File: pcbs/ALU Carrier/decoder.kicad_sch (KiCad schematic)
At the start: 19 parts, among them U2001 74HC138, U2002 74HC14, U2003 74HC08

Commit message: Fix indicators
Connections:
- net +5V: now also D2001.2 (A), D2002.2 (A), D2003.2 (A), D2004.2 (A), D2005.2 (A), D2006.2 (A), D2007.2 (A), D2008.2 (A)
- net GND: no longer D2001.1 (K), D2002.1 (K), D2003.1 (K), D2004.1 (K), D2005.1 (K), D2006.1 (K), D2007.1 (K), D2008.1 (K)
- net at R2005.1: now also D2005.1 (K); no longer D2005.2 (A)
- net at R2006.1: now also D2006.1 (K); no longer D2006.2 (A)
- net at R2004.1: now also D2004.1 (K); no longer D2004.2 (A)
- net at R2007.1: now also D2007.1 (K); no longer D2007.2 (A)
- net at R2008.1: now also D2008.1 (K); no longer D2008.2 (A)
- net at R2001.1: now also D2001.1 (K); no longer D2001.2 (A)
- net at R2002.1: now also D2002.1 (K); no longer D2002.2 (A)
- net at R2003.1: now also D2003.1 (K); no longer D2003.2 (A)
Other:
- moved on the sheet: D2001, D2002, D2003, D2004, D2005, D2006, D2007, D2008
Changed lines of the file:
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@@
 	(symbol
 		(lib_id "Device:LED")
-		(at 152.4 90.17 90)
+		(at 152.4 90.17 270)
 		(unit 1)
 		(exclude_from_sim no)
@@
 		(fields_autoplaced yes)
 		(property "Reference" "D2005"
-			(at 159.385 91.7575 0)
-			(effects
-				(font
-					(size 1.27 1.27)
-				)
+			(at 154.94 87.3124 90)
+			(effects
+				(font
+					(size 1.27 1.27)
+				)
+				(justify left)
 			)
 		)
 		(property "Value" "Blue"
-			(at 156.845 91.7575 0)
-			(effects
-				(font
-					(size 1.27 1.27)
-				)
+			(at 154.94 89.8524 90)
+			(effects
+				(font
+					(size 1.27 1.27)
+				)
+				(justify left)
 			)
 		)
@@
 	(symbol
 		(lib_id "Device:LED")
-		(at 165.1 90.17 90)
+		(at 165.1 90.17 270)
 		(unit 1)
 		(exclude_from_sim no)
@@
 		(fields_autoplaced yes)
 		(property "Reference" "D2006"
-			(at 172.085 91.7575 0)
-			(effects
-				(font
-					(size 1.27 1.27)
-				)
+			(at 167.64 87.3124 90)
+			(effects
+				(font
+					(size 1.27 1.27)
+				)
+				(justify left)
 			)
 		)
 		(property "Value" "Blue"
-			(at 169.545 91.7575 0)
-			(effects
-				(font
-					(size 1.27 1.27)
-				)
+			(at 167.64 89.8524 90)
+			(effects
+				(font
+					(size 1.27 1.27)
+				)
+				(justify left)
 			)
 		)
@@
 				(path "/2be9e5f9-941e-4c29-a733-4c8d2e8b8610/76c82fde-9a27-48e2-82d2-e603579339ec"
 					(reference "D2006")
-					(unit 1)
-				)
-			)
-		)
-	)
-	(symbol
-		(lib_id "power:GND")
-		(at 101.6 101.6 0)
-		(unit 1)
-		(exclude_from_sim no)
-		(in_bom yes)
-		(on_board yes)
-		(dnp no)
-		(fields_autoplaced yes)
-		(property "Reference" "#PWR02003"
-			(at 101.6 107.95 0)
-			(effects
-				(font
-					(size 1.27 1.27)
-				)
-				(hide yes)
-			)
-		)
-		(property "Value" "GND"
-			(at 101.6 106.68 0)
-			(effects
-				(font
-					(size 1.27 1.27)
-				)
-			)
-		)
-		(property "Footprint" ""
-			(at 101.6 101.6 0)
-			(effects
-				(font
-					(size 1.27 1.27)
-				)
-				(hide yes)
-			)
-		)
-		(property "Datasheet" ""
-			(at 101.6 101.6 0)
-			(effects
-				(font
-					(size 1.27 1.27)
-				)
-				(hide yes)
-			)
-		)
-		(property "Description" "Power symbol creates a global label with name \"GND\" , ground"
-			(at 101.6 101.6 0)
-			(effects
-				(font
-					(size 1.27 1.27)
-				)
-				(hide yes)
-			)
-		)
-		(pin "1"
-		)
-		(instances
-			(project ""
-				(path "/2be9e5f9-941e-4c29-a733-4c8d2e8b8610/76c82fde-9a27-48e2-82d2-e603579339ec"
-					(reference "#PWR02003")
 					(unit 1)
 				)
@@
 	(symbol
 		(lib_id "Device:LED")
-		(at 190.5 90.17 90)
+		(at 190.5 90.17 270)
 		(unit 1)
 		(exclude_from_sim no)
@@
 		(fields_autoplaced yes)
 		(property "Reference" "D2008"
-			(at 197.485 91.7575 0)
-			(effects
-				(font
-					(size 1.27 1.27)
-				)
+			(at 193.04 87.3124 90)
+			(effects
+				(font
+					(size 1.27 1.27)
+				)
+				(justify left)
 			)
 		)
 		(property "Value" "Blue"
-			(at 194.945 91.7575 0)
-			(effects
-				(font
-					(size 1.27 1.27)
-				)
+			(at 193.04 89.8524 90)
+			(effects
+				(font
+					(size 1.27 1.27)
+				)
+				(justify left)
 			)
 		)
@@
 	(symbol
 		(lib_id "Device:LED")
-		(at 101.6 90.17 90)
+		(at 101.6 90.17 270)
 		(unit 1)
 		(exclude_from_sim no)
@@
 		(fields_autoplaced yes)
 		(property "Reference" "D2001"
-			(at 108.585 91.7575 0)
-			(effects
-				(font
-					(size 1.27 1.27)
-				)
+			(at 104.14 87.3124 90)
+			(effects
+				(font
+					(size 1.27 1.27)
+				)
+				(justify left)
 			)
 		)
 		(property "Value" "Blue"
-			(at 106.045 91.7575 0)
-			(effects
-				(font
-					(size 1.27 1.27)
-				)
+			(at 104.14 89.8524 90)
+			(effects
+				(font
+					(size 1.27 1.27)
+				)
+				(justify left)
 			)
 		)
@@
 	)
 	(symbol
+		(lib_id "power:+5V")
+		(at 101.6 101.6 180)
+		(unit 1)
+		(exclude_from_sim no)
+		(in_bom yes)
+		(on_board yes)
+		(dnp no)
+		(fields_autoplaced yes)
+		(property "Reference" "#PWR02003"
+			(at 101.6 97.79 0)
+			(effects
+				(font
+					(size 1.27 1.27)
+				)
+				(hide yes)
+			)
+		)
+		(property "Value" "+5V"
+			(at 101.6 106.68 0)
+			(effects
+				(font
+					(size 1.27 1.27)
+				)
+			)
+		)
+		(property "Footprint" ""
+			(at 101.6 101.6 0)
+			(effects
+				(font
+					(size 1.27 1.27)
+				)
+				(hide yes)
+			)
+		)
+		(property "Datasheet" ""
+			(at 101.6 101.6 0)
+			(effects
+				(font
+					(size 1.27 1.27)
+				)
+				(hide yes)
+			)
+		)
+		(property "Description" "Power symbol creates a global label with name \"+5V\""
+			(at 101.6 101.6 0)
+			(effects
+				(font
+					(size 1.27 1.27)
+				)
+				(hide yes)
+			)
+		)
+		(pin "1"
+		)
+		(instances
+			(project "ALU Carrier"
+				(path "/2be9e5f9-941e-4c29-a733-4c8d2e8b8610/76c82fde-9a27-48e2-82d2-e603579339ec"
+					(reference "#PWR02003")
+					(unit 1)
+				)
+			)
+		)
+	)
+	(symbol
 		(lib_id "Device:LED")
-		(at 139.7 90.17 90)
+		(at 139.7 90.17 270)
 		(unit 1)
 		(exclude_from_sim no)
@@
 		(fields_autoplaced yes)
 		(property "Reference" "D2004"
-			(at 146.685 91.7575 0)
-			(effects
-				(font
-					(size 1.27 1.27)
-				)
+			(at 142.24 87.3124 90)
+			(effects
+				(font
+					(size 1.27 1.27)
+				)
+				(justify left)
 			)
 		)
 		(property "Value" "Red"
-			(at 144.145 91.7575 0)
-			(effects
-				(font
-					(size 1.27 1.27)
-				)
+			(at 142.24 89.8524 90)
+			(effects
+				(font
+					(size 1.27 1.27)
+				)
+				(justify left)
 			)
 		)
@@
 	(symbol
 		(lib_id "Device:LED")
-		(at 114.3 90.17 90)
+		(at 114.3 90.17 270)
 		(unit 1)
 		(exclude_from_sim no)
@@
 		(fields_autoplaced yes)
 		(property "Reference" "D2002"
-			(at 121.285 91.7575 0)
-			(effects
-				(font
-					(size 1.27 1.27)
-				)
+			(at 116.84 87.3124 90)
+			(effects
+				(font
+					(size 1.27 1.27)
+				)
+				(justify left)
 			)
 		)
 		(property "Value" "Blue"
-			(at 118.745 91.7575 0)
-			(effects
-				(font
-					(size 1.27 1.27)
-				)
+			(at 116.84 89.8524 90)
+			(effects
+				(font
+					(size 1.27 1.27)
+				)
+				(justify left)
 			)
 		)
@@
 	(symbol
 		(lib_id "Device:LED")
-		(at 127 90.17 90)
+		(at 127 90.17 270)
 		(unit 1)
 		(exclude_from_sim no)
@@
 		(fields_autoplaced yes)
 		(property "Reference" "D2003"
-			(at 133.985 91.7575 0)
-			(effects
-				(font
-					(size 1.27 1.27)
-				)
+			(at 129.54 87.3124 90)
+			(effects
+				(font
+					(size 1.27 1.27)
+				)
+				(justify left)
 			)
 		)
 		(property "Value" "Red"
-			(at 131.445 91.7575 0)
-			(effects
-				(font
-					(size 1.27 1.27)
-				)
+			(at 129.54 89.8524 90)
+			(effects
+				(font
+					(size 1.27 1.27)
+				)
+				(justify left)
 			)
 		)
@@
 	(symbol
 		(lib_id "Device:LED")
-		(at 177.8 90.17 90)
+		(at 177.8 90.17 270)
 		(unit 1)
 		(exclude_from_sim no)
@@
 		(fields_autoplaced yes)
 		(property "Reference" "D2007"
-			(at 184.785 91.7575 0)
-			(effects
-				(font
-					(size 1.27 1.27)
-				)
+			(at 180.34 87.3124 90)
+			(effects
+				(font
+					(size 1.27 1.27)
+				)
+				(justify left)
 			)
 		)
 		(property "Value" "Blue"
-			(at 182.245 91.7575 0)
-			(effects
-				(font
-					(size 1.27 1.27)
-				)
-			)
-		)
+			(at 180.34 89.8524 90)
+			(effects
+				(font
+					(size 1.27 1.27)
+				)
+				(justify left)
+			)
+		)

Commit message: Refactor
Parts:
- removed U2002: 74HC14, Package_SO:SOIC-14_3.9x8.7mm_P1.27mm, symbol 74xx:74HC14
- removed U2003: 74HC08, Package_SO:SOIC-14_3.9x8.7mm_P1.27mm, symbol 74xx:74LS08
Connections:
- no-connect marks 7 -> 0

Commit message: Thinking some more
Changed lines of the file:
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@@
 		)
 	)
-	(hierarchical_label "I[0..15]"
+	(hierarchical_label "I[0..3]"
 		(shape input)
 		(at 25.4 25.4 180)

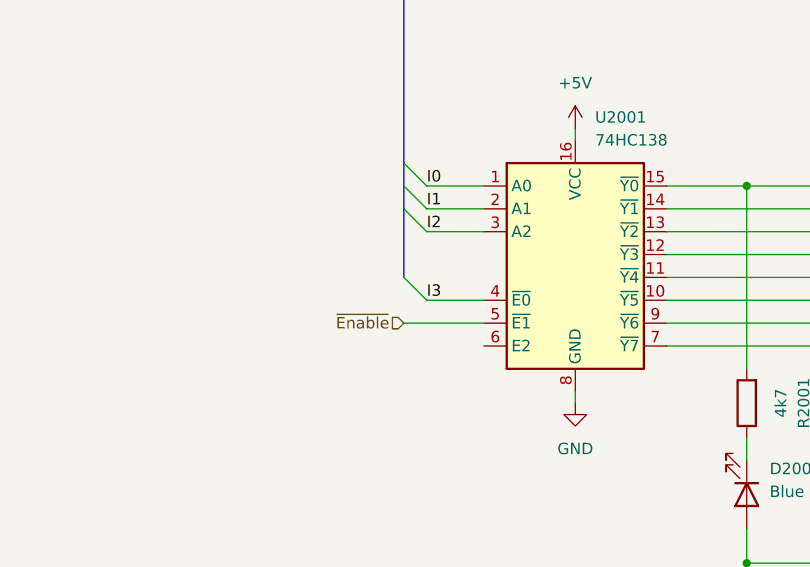
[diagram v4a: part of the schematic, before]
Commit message: Spotted nasty error in enable logic
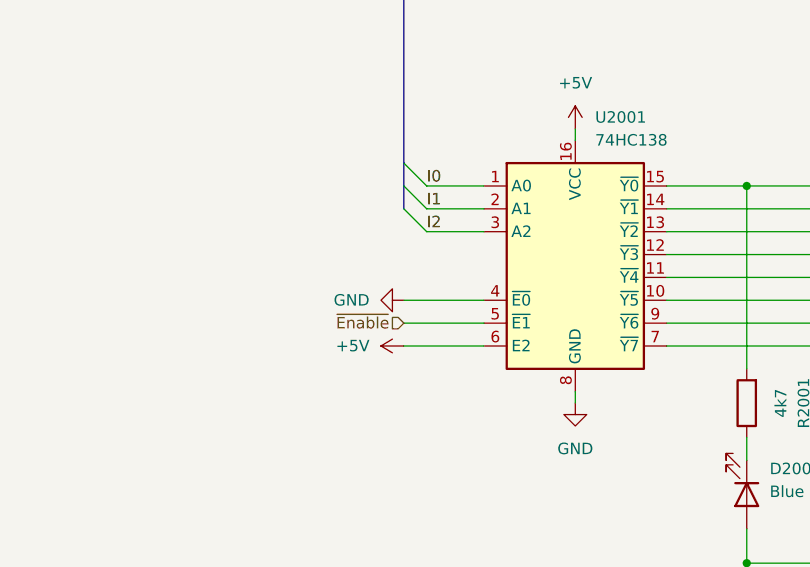
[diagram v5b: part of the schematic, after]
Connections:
- net I3 is gone; now on net GND: U2001.4 (~{E0})
- net +5V: now also U2001.6 (E2)
